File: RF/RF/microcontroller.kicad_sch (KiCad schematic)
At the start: 21 parts, among them IC201 CC1110F16RHHR

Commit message: added external memory
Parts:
- added C210: 0.1uF, Capacitor_SMD:C_0603_1608Metric_Pad1.08x0.95mm_HandSolder, symbol Device:C
- added C211: 0.01uF, Capacitor_SMD:C_0603_1608Metric_Pad1.08x0.95mm_HandSolder, symbol Device:C
- added R208: 0R, Resistor_SMD:R_0603_1608Metric_Pad0.98x0.95mm_HandSolder, symbol Device:R
- added Y201: TG2520SMN 27.000M-MCGNNM3, SamacSys_Parts:TG2520SMN25000MMCGNNM3, symbol SamacSys_Parts:TG2520SMN_25.000M-MCGNNM3
- C201, C202, C203, C204, C205, C206, C207, C208, C209: footprint (none) -> Capacitor_SMD:C_0603_1608Metric_Pad1.08x0.95mm_HandSolder
- D201, D202: footprint (none) -> LED_SMD:LED_0603_1608Metric_Pad1.05x0.95mm_HandSolder
- FB201: footprint (none) -> Inductor_SMD:L_0603_1608Metric_Pad1.05x0.95mm_HandSolder
- IC201: footprint QFN50P600X600X100-37N-D -> SamacSys_Parts:QFN50P600X600X100-37N-D
- R201, R202, R203, R204, R205, R206, R207: footprint (none) -> Resistor_SMD:R_0603_1608Metric_Pad0.98x0.95mm_HandSolder
- TP201: footprint (none) -> TestPoint:TestPoint_Loop_D3.50mm_Drill1.4mm_Beaded
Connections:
- net +3.3V: now also R208.2; no longer FB201.1
- net +3.3VA: now also C210.1, Y201.4 (VCC)
- net GND: now also C210.2, Y201.2 (GND)
- net ~{FLASH_CS}: now reaches IC201.14 (P2_0)
- net AN0 renamed AIN0
- net AN1: no longer names the net of IC201.6 (P0_1)
- net CC_SOC_OSC renamed CC_SOC_OC
- net CC_SOC_OC: now also C211.2
- net UART1_CTS renamed MISO
- net UART1_RTS renamed MOSI
- net UART1_RX renamed SCK
- net UART1_TX renamed ~{SRAM_CS}
- new net: C211.1, Y201.3 (OUT)
- new net: FB201.1, R208.1
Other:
- note added: "CC1110F16 MICROCONTROLLER/TRANSCIVER"
- note added: "Clipped Sine Wave Oscillator 27MHz"
- note added: "Remove OR resistor to pull RESET_N LOW TODO: Add a switch instead of this"
- note removed: "Remove OR resistor to pull RESET_N LOW"
- moved on the sheet: C209, D201, D202, IC201, R201, R202, R203, R204, R205, R206, R207, TP201

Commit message: RF: Push for schematic capture review version 1.0
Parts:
- removed R204: 0R, Resistor_SMD:R_0603_1608Metric_Pad0.98x0.95mm_HandSolder, symbol Device:R
- added J201: Conn_01x02, Connector_PinHeader_1.27mm:PinHeader_1x02_P1.27mm_Vertical, symbol Connector_Generic:Conn_01x02
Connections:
- net +3.3VA: now also J201.2 (Pin_2)
- net at IC201.31 (RESET_N), R205.1: now also J201.1 (Pin_1)
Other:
- note added: "CC1110F8/32 are drop in replacements"
- note added: "Remove Jumper resistor to pull RESET_N LOW"
- note removed: "Remove OR resistor to pull RESET_N LOW TODO: Add a switch instead of this"
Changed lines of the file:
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@@
   (junction (at 62.992 50.8) (diameter 0) (color 0 0 0 0)
   )
-  (junction (at 213.614 52.324) (diameter 0) (color 0 0 0 0)
-  )
   (junction (at 85.344 43.18) (diameter 0) (color 0 0 0 0)
   )
@@
   )
   (junction (at 218.44 82.804) (diameter 0) (color 0 0 0 0)
+  )
+  (junction (at 219.456 52.324) (diameter 0) (color 0 0 0 0)
   )
   (junction (at 59.69 43.18) (diameter 0) (color 0 0 0 0)
@@
     (stroke (width 0) (type default))
   )
-  (wire (pts (xy 202.692 52.324) (xy 200.66 52.324))
+  (wire (pts (xy 200.66 52.324) (xy 209.042 52.324))
     (stroke (width 0) (type default))
   )
@@
     (stroke (width 0) (type default))
   )
-  (wire (pts (xy 210.312 52.324) (xy 213.614 52.324))
-    (stroke (width 0) (type default))
-  )
   (wire (pts (xy 191.262 33.782) (xy 185.674 33.782))
     (stroke (width 0) (type default))
@@
     (stroke (width 0) (type default))
   )
-  (wire (pts (xy 213.614 54.864) (xy 186.182 54.864))
+  (wire (pts (xy 219.456 54.864) (xy 186.182 54.864))
     (stroke (width 0) (type default))
   )
@@
     (stroke (width 0) (type default))
   )
-  (wire (pts (xy 213.614 52.324) (xy 213.614 54.864))
+  (wire (pts (xy 219.456 41.91) (xy 219.456 52.324))
     (stroke (width 0) (type default))
   )
@@
     (stroke (width 0) (type default))
   )
-  (wire (pts (xy 213.614 42.418) (xy 213.614 52.324))
-    (stroke (width 0) (type default))
-  )
   (wire (pts (xy 149.86 85.344) (xy 155.702 85.344))
     (stroke (width 0) (type default))
@@
     (stroke (width 0) (type default))
   )
+  (wire (pts (xy 211.582 52.324) (xy 219.456 52.324))
+    (stroke (width 0) (type default))
+  )
   (wire (pts (xy 176.022 130.302) (xy 192.532 130.302))
     (stroke (width 0) (type default))
@@
     (stroke (width 0) (type default))
   )
+  (wire (pts (xy 219.456 52.324) (xy 219.456 54.864))
+    (stroke (width 0) (type default))
+  )
   (wire (pts (xy 218.44 81.28) (xy 218.44 82.804))
     (stroke (width 0) (type default))
@@
   )
   (rectangle (start 120.65 14.478) (end 262.89 165.1)
-    (stroke (width 0) (type default))
+    (stroke (width 0.5) (type default))
     (fill (type none))
   )
   (rectangle (start 26.924 13.462) (end 103.886 63.246)
-    (stroke (width 0) (type default))
+    (stroke (width 0.5) (type default))
     (fill (type none))
   )
   (rectangle (start 27.178 78.74) (end 101.854 115.316)
-    (stroke (width 0) (type default))
+    (stroke (width 0.5) (type default))
     (fill (type none))
   )
-  (text "Remove OR resistor to pull RESET_N LOW\nTODO: Add a switch instead of this\n"
-    (at 204.216 59.182 0)
+  (text "CC1110F8/32 are drop in replacements" (at 189.23 108.458 0)
+    (effects (font (size 1.27 1.27)) (justify left bottom))
+  )
+  (text "Remove Jumper resistor to pull RESET_N LOW\n\n" (at 204.216 59.182 0)
     (effects (font (face "KiCad Font") (size 1.27 1.27)) (justify left bottom))
   )
@@
     )
   )
+  (symbol (lib_id "Connector_Generic:Conn_01x02") (at 209.042 47.244 90) (unit 1)
+    (in_bom yes) (on_board yes) (dnp no)
+    (property "Reference" "J201" (at 208.026 43.18 90)
+      (effects (font (size 1.27 1.27)) (justify right))
+    )
+    (property "Value" "Conn_01x02" (at 204.978 44.958 90)
+      (effects (font (size 1.27 1.27)) (justify right))
+    )
+    (property "Footprint" "Connector_PinHeader_1.27mm:PinHeader_1x02_P1.27mm_Vertical" (at 209.042 47.244 0)
+      (effects (font (size 1.27 1.27)) hide)
+    )
+    (property "Datasheet" "~" (at 209.042 47.244 0)
+      (effects (font (size 1.27 1.27)) hide)
+    )
+    (pin "1")
+    (pin "2")
+    (instances
+      (project "RF"
+        (path "/51251c4d-d12e-4de3-8dd9-04d485d7d417/e871939a-46ea-46b5-bf60-7bb94b71eea8"
+          (reference "J201") (unit 1)
+        )
+      )
+    )
+  )
   (symbol (lib_id "Device:R") (at 229.616 91.948 0) (unit 1)
     (in_bom yes) (on_board yes) (dnp no)
@@
         (path "/51251c4d-d12e-4de3-8dd9-04d485d7d417/e871939a-46ea-46b5-bf60-7bb94b71eea8"
           (reference "C209") (unit 1)
-        )
-      )
-    )
-  )
-  (symbol (lib_id "Device:R") (at 206.502 52.324 90) (unit 1)
-    (in_bom yes) (on_board yes) (dnp no) (fields_autoplaced)
-    (property "Reference" "R204" (at 206.502 48.2981 90)
-      (effects (font (size 1.27 1.27)))
-    )
-    (property "Value" "0R" (at 206.502 50.2191 90)
-      (effects (font (size 1.27 1.27)))
-    )
-    (property "Footprint" "Resistor_SMD:R_0603_1608Metric_Pad0.98x0.95mm_HandSolder" (at 206.502 54.102 90)
-      (effects (font (size 1.27 1.27)) hide)
-    )
-    (property "Datasheet" "~" (at 206.502 52.324 0)
-      (effects (font (size 1.27 1.27)) hide)
-    )
-    (pin "1")
-    (pin "2")
-    (instances
-      (project "RF"
-        (path "/51251c4d-d12e-4de3-8dd9-04d485d7d417/e871939a-46ea-46b5-bf60-7bb94b71eea8"
-          (reference "R204") (unit 1)
         )
       )
@@
     )
   )
-  (symbol (lib_id "power:+3.3VA") (at 213.614 42.418 0) (unit 1)
-    (in_bom yes) (on_board yes) (dnp no)
-    (property "Reference" "#PWR0207" (at 213.614 46.228 0)
-      (effects (font (size 1.27 1.27)) hide)
-    )
-    (property "Value" "+3.3VA" (at 218.44 41.91 0)
-      (effects (font (size 1.27 1.27)))
-    )
-    (property "Footprint" "" (at 213.614 42.418 0)
-      (effects (font (size 1.27 1.27)) hide)
-    )
-    (property "Datasheet" "" (at 213.614 42.418 0)
-      (effects (font (size 1.27 1.27)) hide)
-    )
+  (symbol (lib_id "power:+3.3VA") (at 219.456 41.91 0) (unit 1)
+    (in_bom yes) (on_board yes) (dnp no)
+    (property "Reference" "#PWR0207" (at 219.456 45.72 0)
+      (effects (font (size 1.27 1.27)) hide)
+    )
+    (property "Value" "+3.3VA" (at 224.282 41.402 0)
+      (effects (font (size 1.27 1.27)))
+    )
+    (property "Footprint" "" (at 219.456 41.91 0)
+      (effects (font (size 1.27 1.27)) hide)
+    )
+    (property "Datasheet" "" (at 219.456 41.91 0)
+      (effects (font (size 1.27 1.27)) hide)
+    )

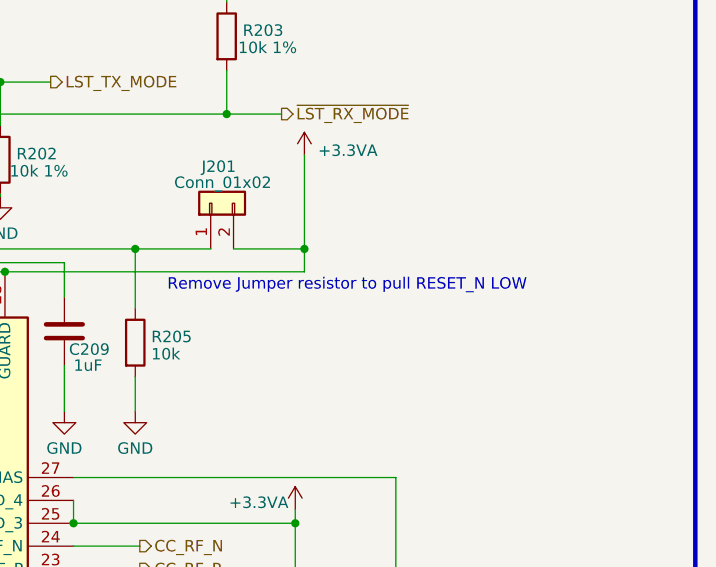
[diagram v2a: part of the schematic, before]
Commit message: added standard connector and some initial layout
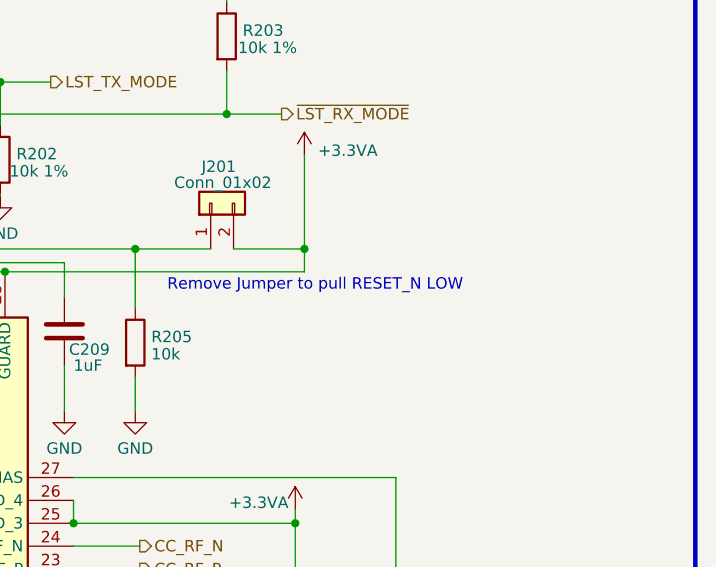
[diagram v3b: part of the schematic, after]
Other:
- note added: "Remove Jumper to pull RESET_N LOW"
- note removed: "Remove Jumper resistor to pull RESET_N LOW"
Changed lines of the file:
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@@
     (effects (font (size 1.27 1.27)) (justify left bottom))
   )
-  (text "Remove Jumper resistor to pull RESET_N LOW\n\n" (at 204.216 59.182 0)
+  (text "Remove Jumper to pull RESET_N LOW\n\n" (at 204.216 59.182 0)
     (effects (font (face "KiCad Font") (size 1.27 1.27)) (justify left bottom))
   )

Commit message: layout rev 1.0
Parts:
- removed TP201: CC_SOC_2, TestPoint:TestPoint_Loop_D3.50mm_Drill1.4mm_Beaded, symbol Connector:TestPoint
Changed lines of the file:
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@@
-    )
-  )
-  (symbol (lib_id "Connector:TestPoint") (at 193.802 95.504 270) (unit 1)
-    (in_bom yes) (on_board yes) (dnp no) (fields_autoplaced)
-    (property "Reference" "TP201" (at 198.501 94.8603 90)
-      (effects (font (size 1.27 1.27)) (justify left))
-    )
-    (property "Value" "CC_SOC_2" (at 198.501 96.7813 90)
-      (effects (font (size 1.27 1.27)) (justify left))
-    )
-    (property "Footprint" "TestPoint:TestPoint_Loop_D3.50mm_Drill1.4mm_Beaded" (at 193.802 100.584 0)
-      (effects (font (size 1.27 1.27)) hide)
-    )
-    (property "Datasheet" "~" (at 193.802 100.584 0)
-      (effects (font (size 1.27 1.27)) hide)
-    )
-    (pin "1")
-    (instances
-      (project "RF"
-        (path "/51251c4d-d12e-4de3-8dd9-04d485d7d417/e871939a-46ea-46b5-bf60-7bb94b71eea8"
-          (reference "TP201") (unit 1)
-        )
-      )
     )
   )
